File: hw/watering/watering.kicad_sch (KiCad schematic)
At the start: 7 parts, among them J2 USB_C_Receptacle

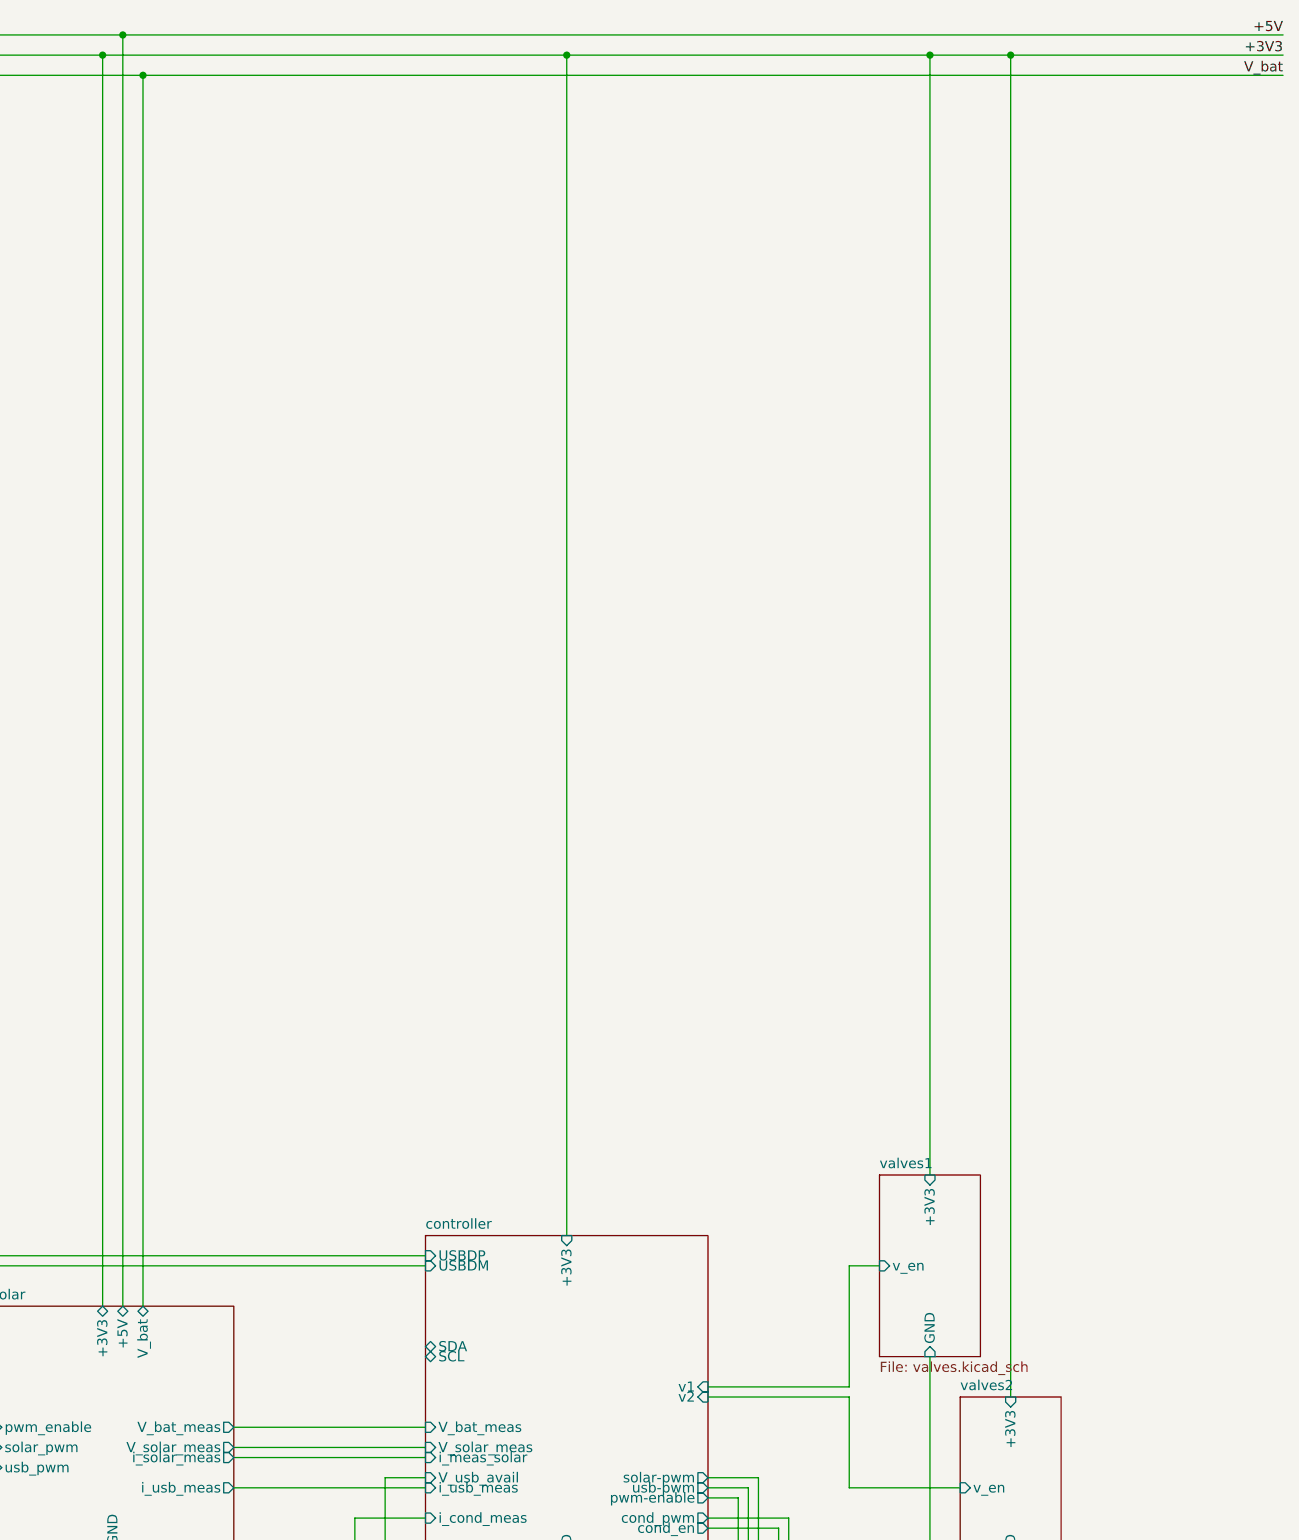
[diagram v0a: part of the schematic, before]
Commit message: reduced pcb size
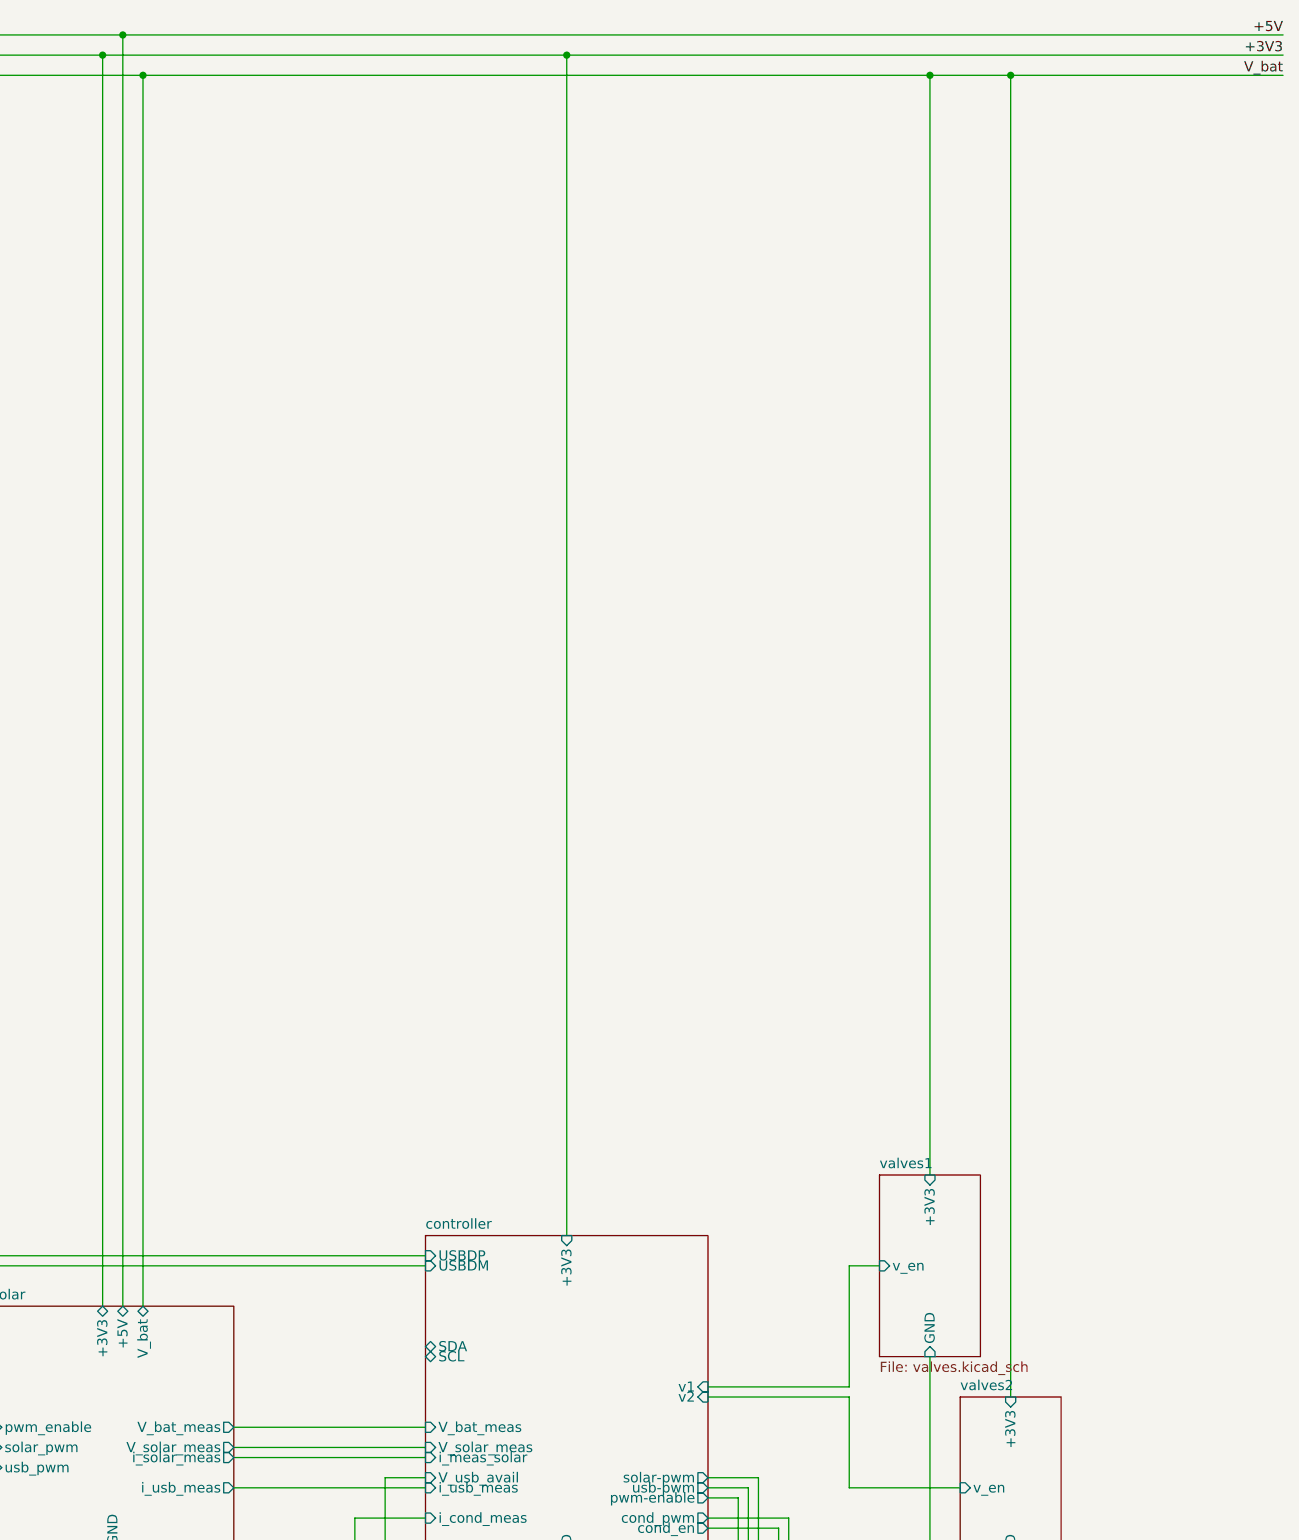
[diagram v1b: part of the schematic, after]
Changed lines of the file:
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@@
-	)
-	(junction
-		(at 358.14 21.59)
-		(diameter 0)
-		(color 0 0 0 0)
 	)
 	(junction
@@
 	)
 	(junction
+		(at 368.3 24.13)
+		(diameter 0)
+		(color 0 0 0 0)
+	)
+	(junction
 		(at 58.42 173.99)
 		(diameter 0)
@@
 	)
 	(junction
-		(at 368.3 21.59)
-		(diameter 0)
-		(color 0 0 0 0)
-	)
-	(junction
 		(at 77.47 179.07)
 		(diameter 0)
@@
 	)
 	(junction
+		(at 358.14 24.13)
+		(diameter 0)
+		(color 0 0 0 0)
+	)
+	(junction
 		(at 113.03 227.33)
 		(diameter 0)
@@
 	(wire
 		(pts
+			(xy 368.3 24.13) (xy 402.59 24.13)
+		)
+		(stroke
+			(width 0)
+			(type default)
+		)
+	)
+	(wire
+		(pts
 			(xy 330.2 200.66) (xy 336.55 200.66)
 		)
@@
 	(wire
 		(pts
+			(xy 358.14 24.13) (xy 368.3 24.13)
+		)
+		(stroke
+			(width 0)
+			(type default)
+		)
+	)
+	(wire
+		(pts
 			(xy 153.67 214.63) (xy 158.75 214.63)
 		)
@@
 	(wire
 		(pts
+			(xy 368.3 24.13) (xy 368.3 190.5)
+		)
+		(stroke
+			(width 0)
+			(type default)
+		)
+	)
+	(wire
+		(pts
 			(xy 58.42 173.99) (xy 95.25 173.99)
 		)
@@
 	(wire
 		(pts
-			(xy 368.3 190.5) (xy 368.3 21.59)
-		)
-		(stroke
-			(width 0)
-			(type default)
-		)
-	)
-	(wire
-		(pts
 			(xy 62.23 167.64) (xy 57.15 167.64)
 		)
@@
 	(wire
 		(pts
+			(xy 358.14 24.13) (xy 358.14 162.56)
+		)
+		(stroke
+			(width 0)
+			(type default)
+		)
+	)
+	(wire
+		(pts
 			(xy 368.3 213.36) (xy 368.3 248.92)
 		)
@@
 	(wire
 		(pts
-			(xy 358.14 162.56) (xy 358.14 21.59)
-		)
-		(stroke
-			(width 0)
-			(type default)
-		)
-	)
-	(wire
-		(pts
-			(xy 259.08 24.13) (xy 402.59 24.13)
-		)
-		(stroke
+			(xy 259.08 24.13) (xy 358.14 24.13)
+		)
+		(stroke

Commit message: - hw   - rewired power input for battery   - some first placing of parts on pcb but no routing - sw   - added example http server from examples to server.cpp, not compilable yet
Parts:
- removed C19: 1u, Capacitor_SMD:C_0603_1608Metric, symbol Device:C
- removed D3: D_TVS_Dual_AAC, Package_TO_SOT_SMD:TSOT-23, symbol Device:D_TVS_Dual_AAC
- removed J2: USB_C_Receptacle, Connector_USB:USB_C_Receptacle_GCT_USB4105-xx-A_16P_TopMnt_Horizontal, symbol Connector:USB_C_Receptacle
- removed R1, R2: 5k1, Resistor_SMD:R_0603_1608Metric, symbol Device:R
- removed R30, R45: 10k, Resistor_SMD:R_0603_1608Metric, symbol Device:R
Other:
- added sheet usb (usb.kicad_sch)
- sheet controller ports: added power-enable; removed none
- sheet solar ports: added power_enable; removed none
